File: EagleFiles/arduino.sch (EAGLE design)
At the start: 23 parts, among them IC2 74250N, IC3 74250N, IC4 74250N, J1 AVR_SPI, U1 ATMEGA168

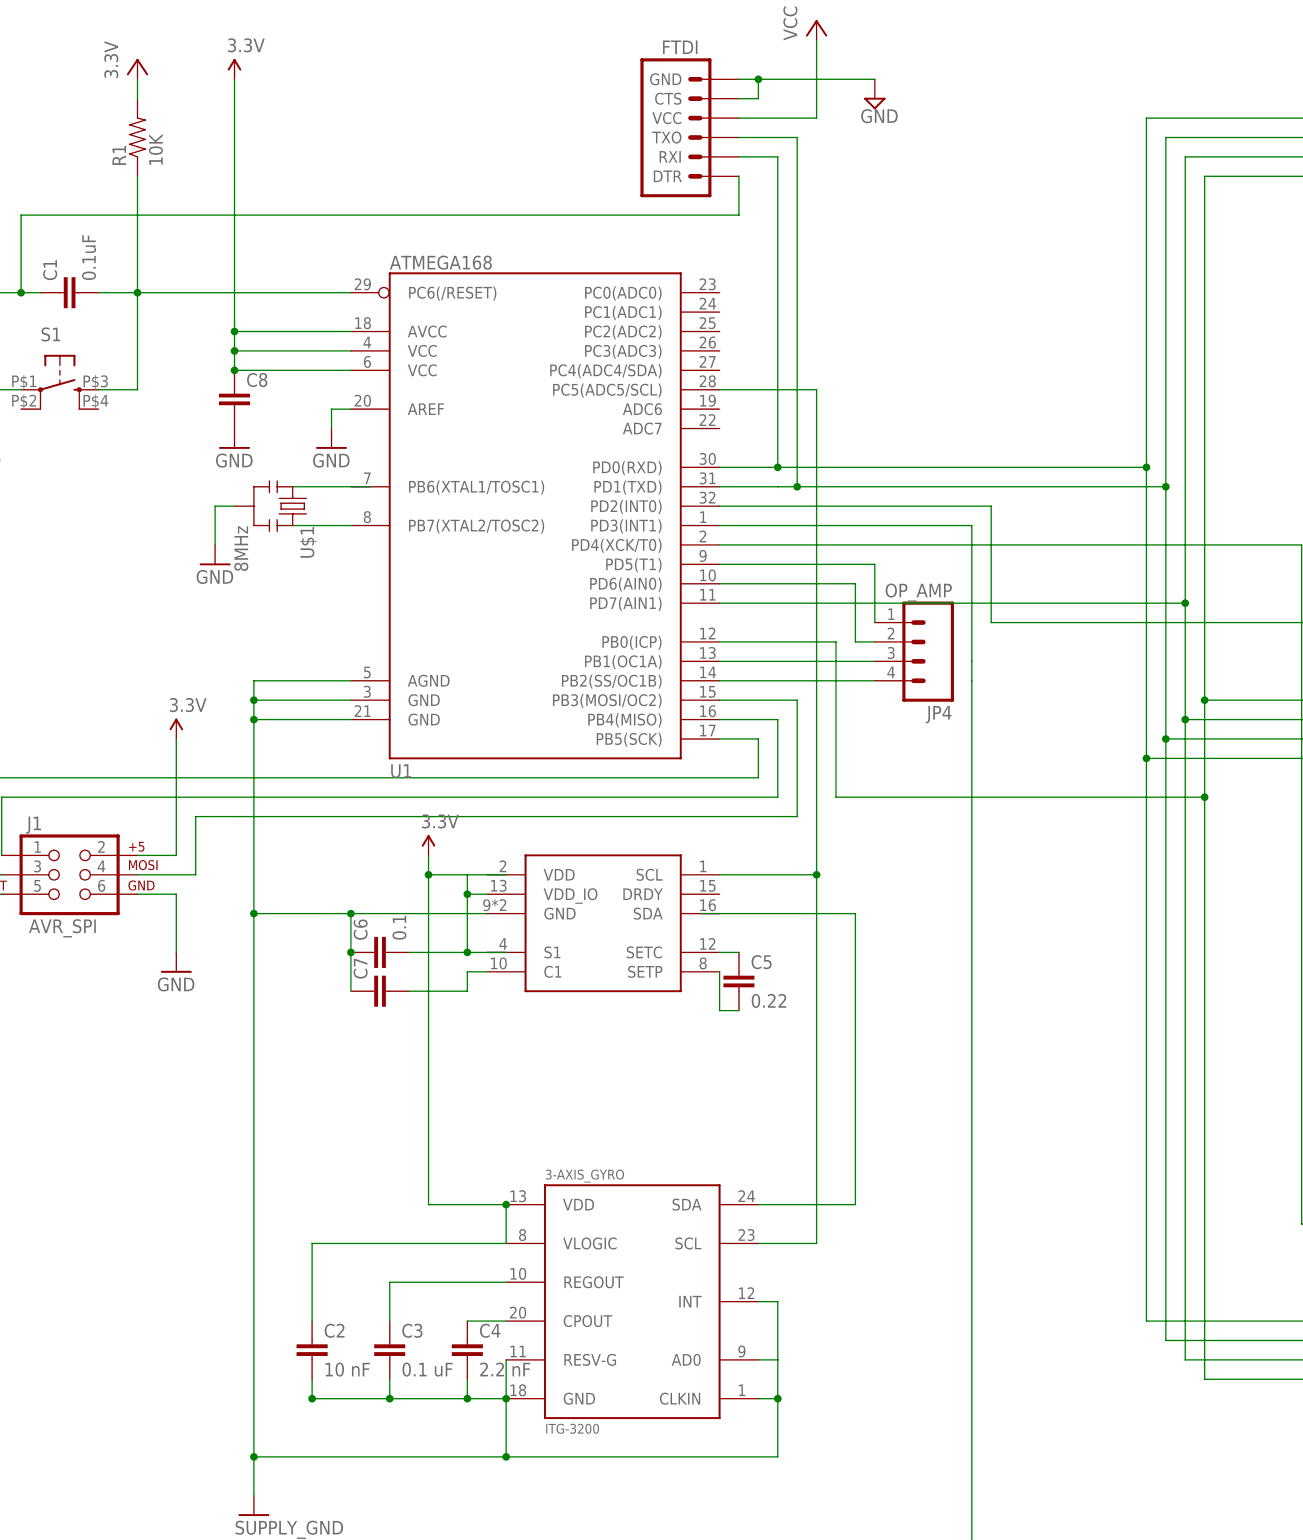
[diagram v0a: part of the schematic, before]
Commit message: made changes suggested by Edrick
- switched ftdi rx/tx times
- added caps to each power line in to ATMEGA
- fixed SDA connection for 12c bus
- fixed gyro connections
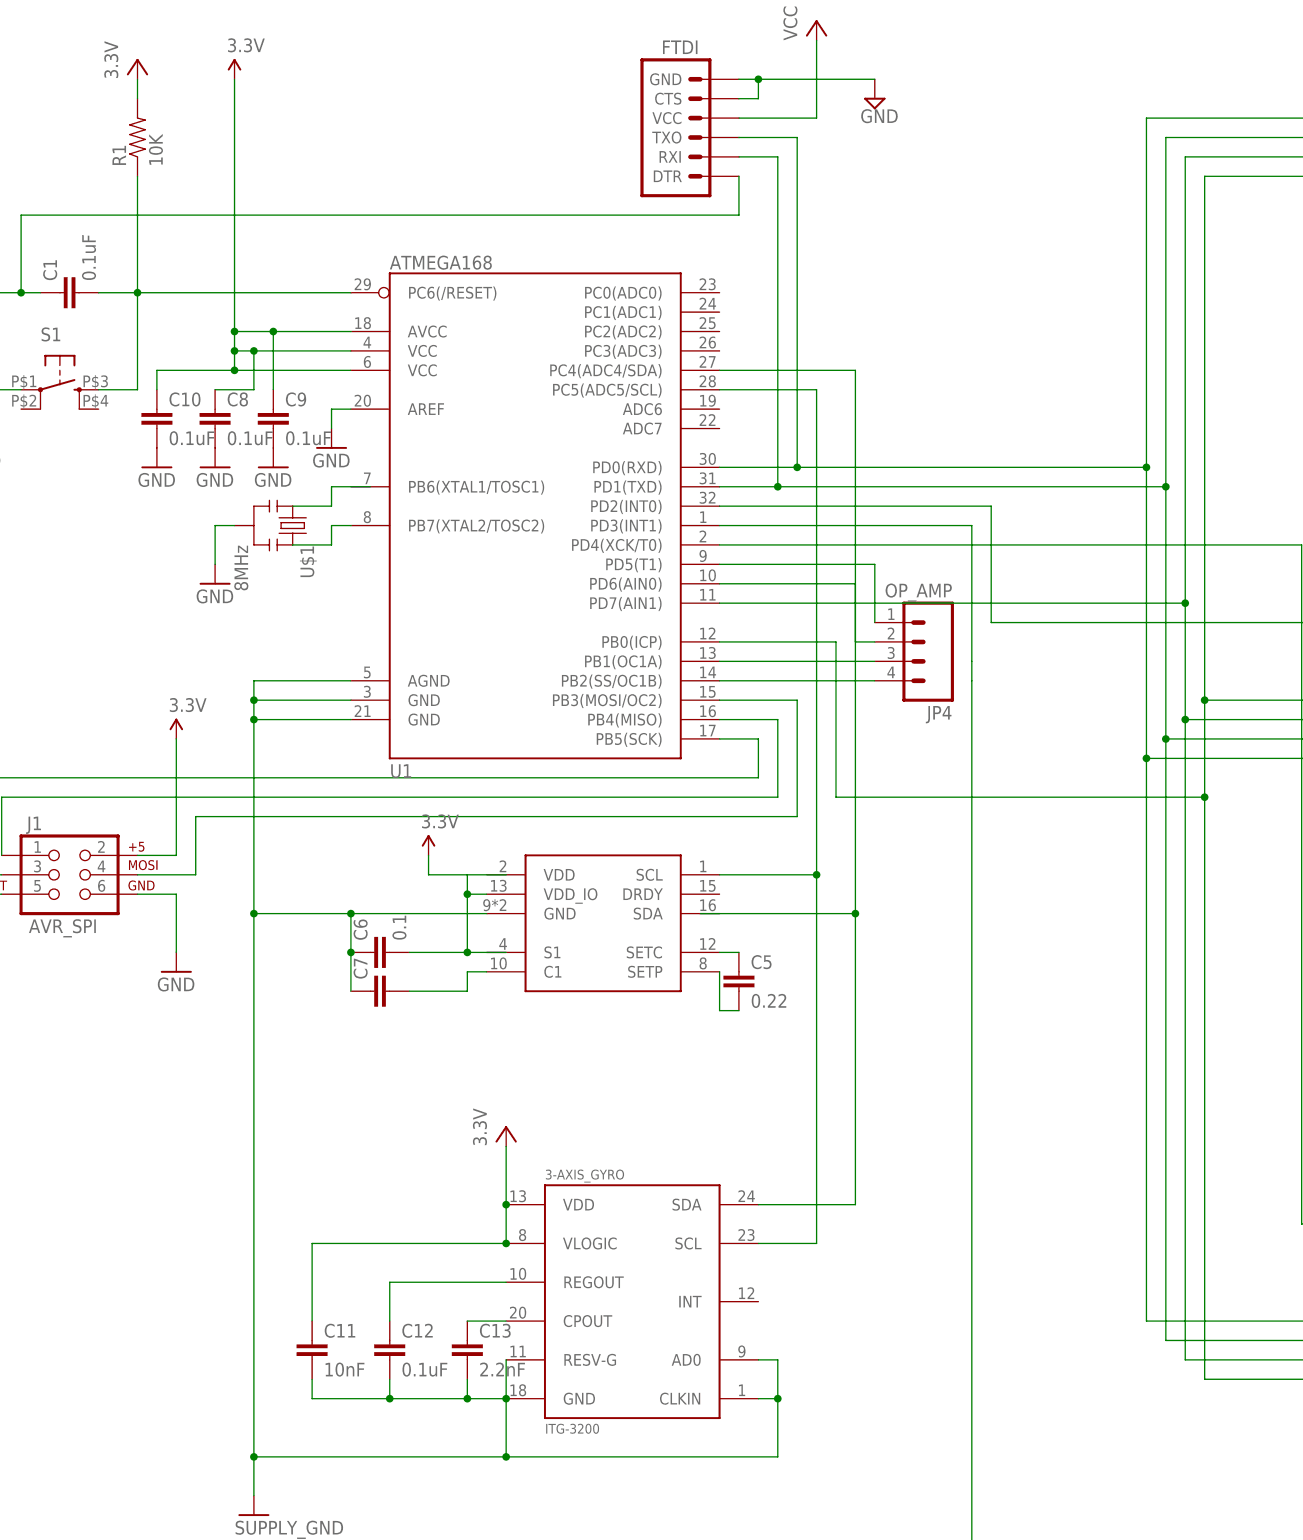
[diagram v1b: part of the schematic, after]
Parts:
- removed C2: 10 nF, SparkFun:CAPPTH
- removed C3: 0.1 uF, SparkFun:CAPPTH
- removed C4: 2.2 nF, SparkFun:CAPPTH
- added C10, C9: 0.1uF, SparkFun:CAP0603-CAP
- added C11: 10nF, SparkFun:CAP0402-CAP
- added C12: 0.1uF, SparkFun:CAP0402-CAP
- added C13: 2.2nF, SparkFun:CAP0402-CAP
- C8: value (none) -> 0.1uF
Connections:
- removed net N$63: FTDI.RXI, IC2A.A, IC3A.A, IC4A.A, U1.PD0(RXD)
- removed net N$66: FTDI.TXO, IC2A.B, IC3A.B, IC4A.B, U1.PD1(TXD)
- new net N$3: FTDI.RXI, IC2A.B, IC3A.B, IC4A.B, U1.PD1(TXD)
- new net N$4: FTDI.TXO, IC2A.A, IC3A.A, IC4A.A, U1.PD0(RXD)
- net GND: now also C10.2, C11.2, C12.2, C13.2, C9.2; no longer 3-AXIS_GYRO.INT, C2.2, C3.2, C4.2
- net N$43: now also U1.PC4(ADC4/SDA)
- net N$64: now also C13.1; no longer C4.1
- net N$65: now also C12.1; no longer C3.1
- net VCC: now also C10.1, C11.1, C9.1; no longer C2.1
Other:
- moved on the sheet: C8, U$1

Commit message: made the fixes
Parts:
- removed IC4: 74250N, 74xx-us:74250N
- added IC1: 4067D, 40xx:4067D
- added R2, R3: 4.7k, SparkFun:RESISTOR
- IC2: value 74250N -> 4067D; device 74xx-us:74250N -> 40xx:4067D
- IC3: value 74250N -> 4067D; device 74xx-eu:74250N -> 40xx:4067D
- JP4: value OP_AMP -> LPF
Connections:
- net GND: now also IC1A.INH, IC2A.INH, IC3A.INH; no longer IC2A.G, IC3A.G, IC4A.G
- net N$1: now also IC1A.X15; no longer IC2A.E15
- net N$10: now also IC1A.X12; no longer IC2A.E12
- net N$11: now also IC1A.X11; no longer IC2A.E11
- net N$12: now also IC1A.X10; no longer IC2A.E10
- net N$13: now also IC1A.X9; no longer IC2A.E9
- net N$14: now also IC1A.X8; no longer IC2A.E8
- net N$15: now also IC1A.X7; no longer IC2A.E7
- net N$16: now also IC1A.X6; no longer IC2A.E6
- net N$17: now also IC1A.X5; no longer IC2A.E5
- net N$18: now also IC1A.X4; no longer IC2A.E4
- net N$19: now also IC1A.X3; no longer IC2A.E3
- net N$2: now also IC1A.C, IC2A.B, IC3A.B; no longer IC2A.C, IC3A.C, IC4A.C
- net N$20: now also IC1A.X2; no longer IC2A.E2
- net N$21: now also IC1A.X1; no longer IC2A.E1
- net N$22: now also IC1A.X0; no longer IC2A.E0
- net N$23: now also IC2A.X15; no longer IC3A.E15
- net N$24: now also IC2A.X14; no longer IC3A.E14
- net N$25: now also IC2A.X13; no longer IC3A.E13
- net N$26: now also IC2A.X12; no longer IC3A.E12
- net N$27: now also IC2A.X11; no longer IC3A.E11
- net N$28: now also IC2A.X10; no longer IC3A.E10
- net N$29: now also IC2A.X9; no longer IC3A.E9
- net N$3: now also IC1A.B, IC2A.C, IC3A.C; no longer IC2A.B, IC3A.B, IC4A.B
- net N$30: now also IC2A.X8; no longer IC3A.E8
- net N$31: now also IC2A.X7; no longer IC3A.E7
- net N$32: now also IC2A.X6; no longer IC3A.E6
- net N$33: now also IC2A.X5; no longer IC3A.E5
- net N$34: now also IC2A.X4; no longer IC3A.E4
- net N$35: now also IC2A.X3; no longer IC3A.E3
- net N$36: now also IC2A.X2; no longer IC3A.E2
- net N$37: now also IC2A.X1; no longer IC3A.E1
- net N$38: now also IC2A.X0; no longer IC3A.E0
- net N$4: now also IC1A.A, IC2A.D, IC3A.D; no longer IC2A.A, IC3A.A, IC4A.A
- net N$41: now also R2.1
- net N$42: now also IC3A.X, U1.PC2(ADC2); no longer IC4A.W, U1.PD3(INT1)
- net N$43: now also R3.1
- net N$46: now also IC3A.X15; no longer IC4A.E15
- net N$47: now also IC3A.X14; no longer IC4A.E14
- net N$48: now also IC3A.X13; no longer IC4A.E13
- net N$49: now also IC3A.X12; no longer IC4A.E12
- net N$5: now also IC1A.X, U1.PC0(ADC0); no longer IC2A.W, U1.PD2(INT0)
- net N$50: now also IC3A.X11; no longer IC4A.E11
- net N$51: now also IC3A.X10; no longer IC4A.E10
- net N$52: now also IC3A.X9; no longer IC4A.E9
- net N$53: now also IC3A.X8; no longer IC4A.E8
- net N$54: now also IC3A.X7; no longer IC4A.E7
- net N$55: now also IC3A.X6; no longer IC4A.E6
- net N$56: now also IC3A.X5; no longer IC4A.E5
- net N$57: now also IC3A.X4; no longer IC4A.E4
- net N$58: now also IC3A.X3; no longer IC4A.E3
- net N$59: now also IC3A.X2; no longer IC4A.E2
- net N$6: now also IC2A.X, U1.PC1(ADC1); no longer IC3A.W, U1.PD4(XCK/T0)
- net N$60: now also IC3A.X1; no longer IC4A.E1
- net N$61: now also IC3A.X0; no longer IC4A.E0
- net N$7: now also IC1A.D, IC2A.A, IC3A.A; no longer IC2A.D, IC3A.D, IC4A.D
- net N$8: now also IC1A.X14; no longer IC2A.E14
- net N$9: now also IC1A.X13; no longer IC2A.E13
- net VCC: now also 3-AXIS_MAG.VDD, R2.2, R3.2
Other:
- moved on the sheet: JP1, JP2, JP3, JP4

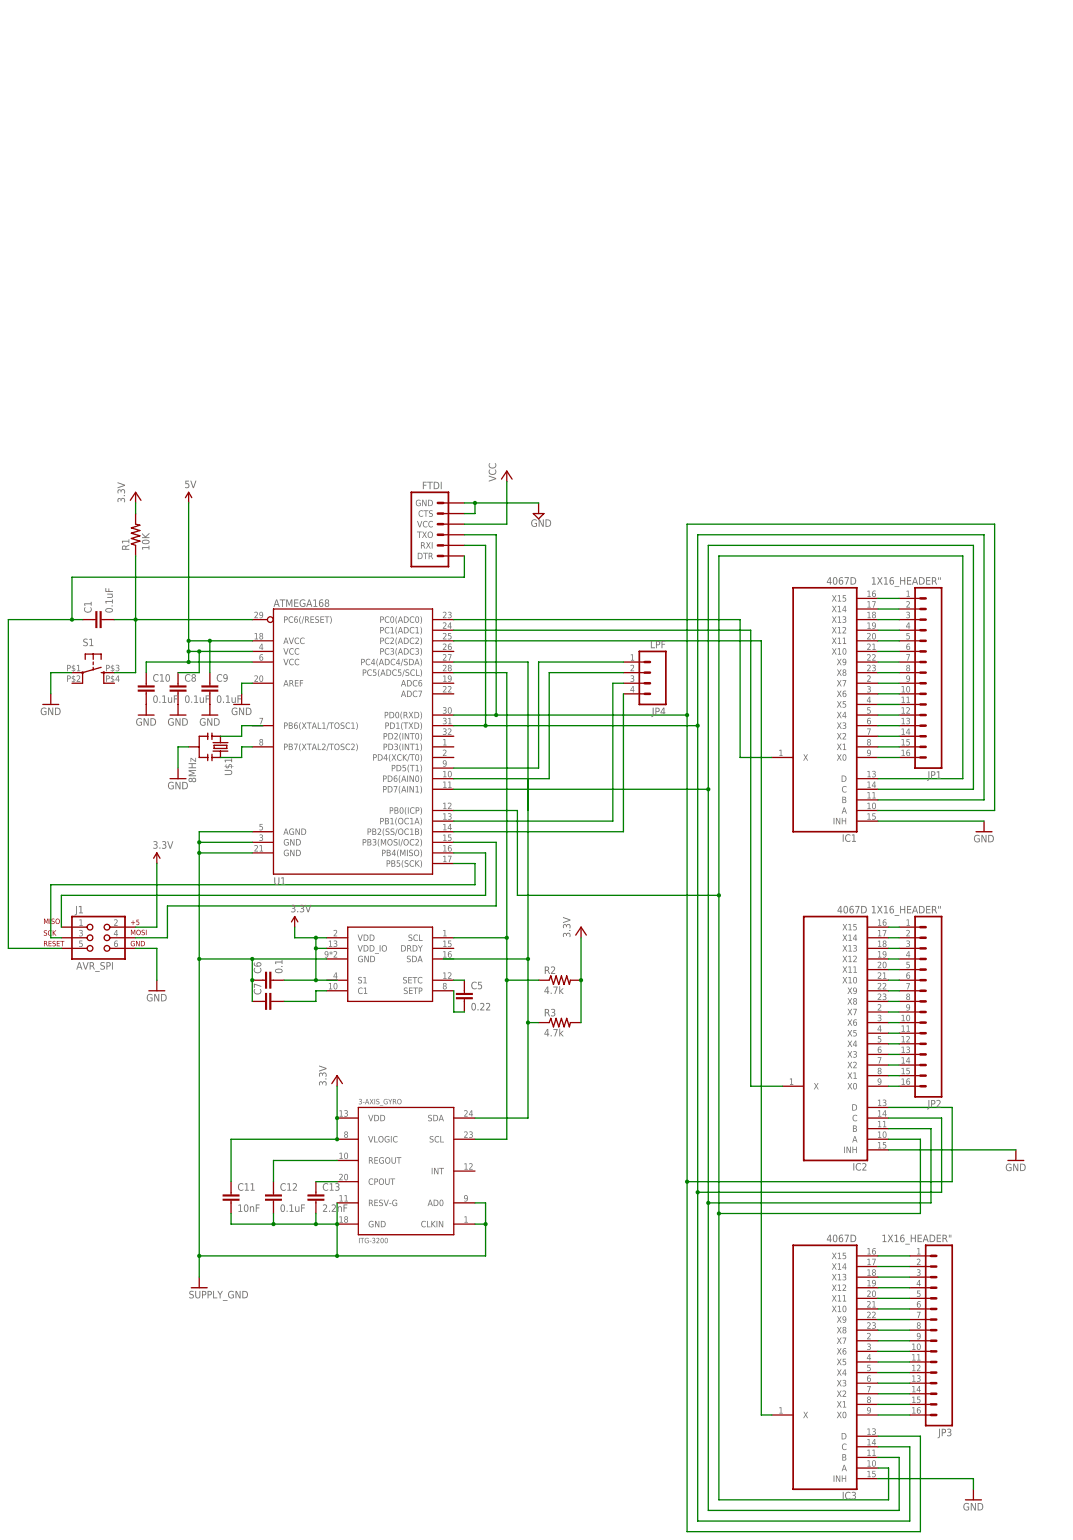
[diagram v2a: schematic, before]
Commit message: added the lpf because forgot that before
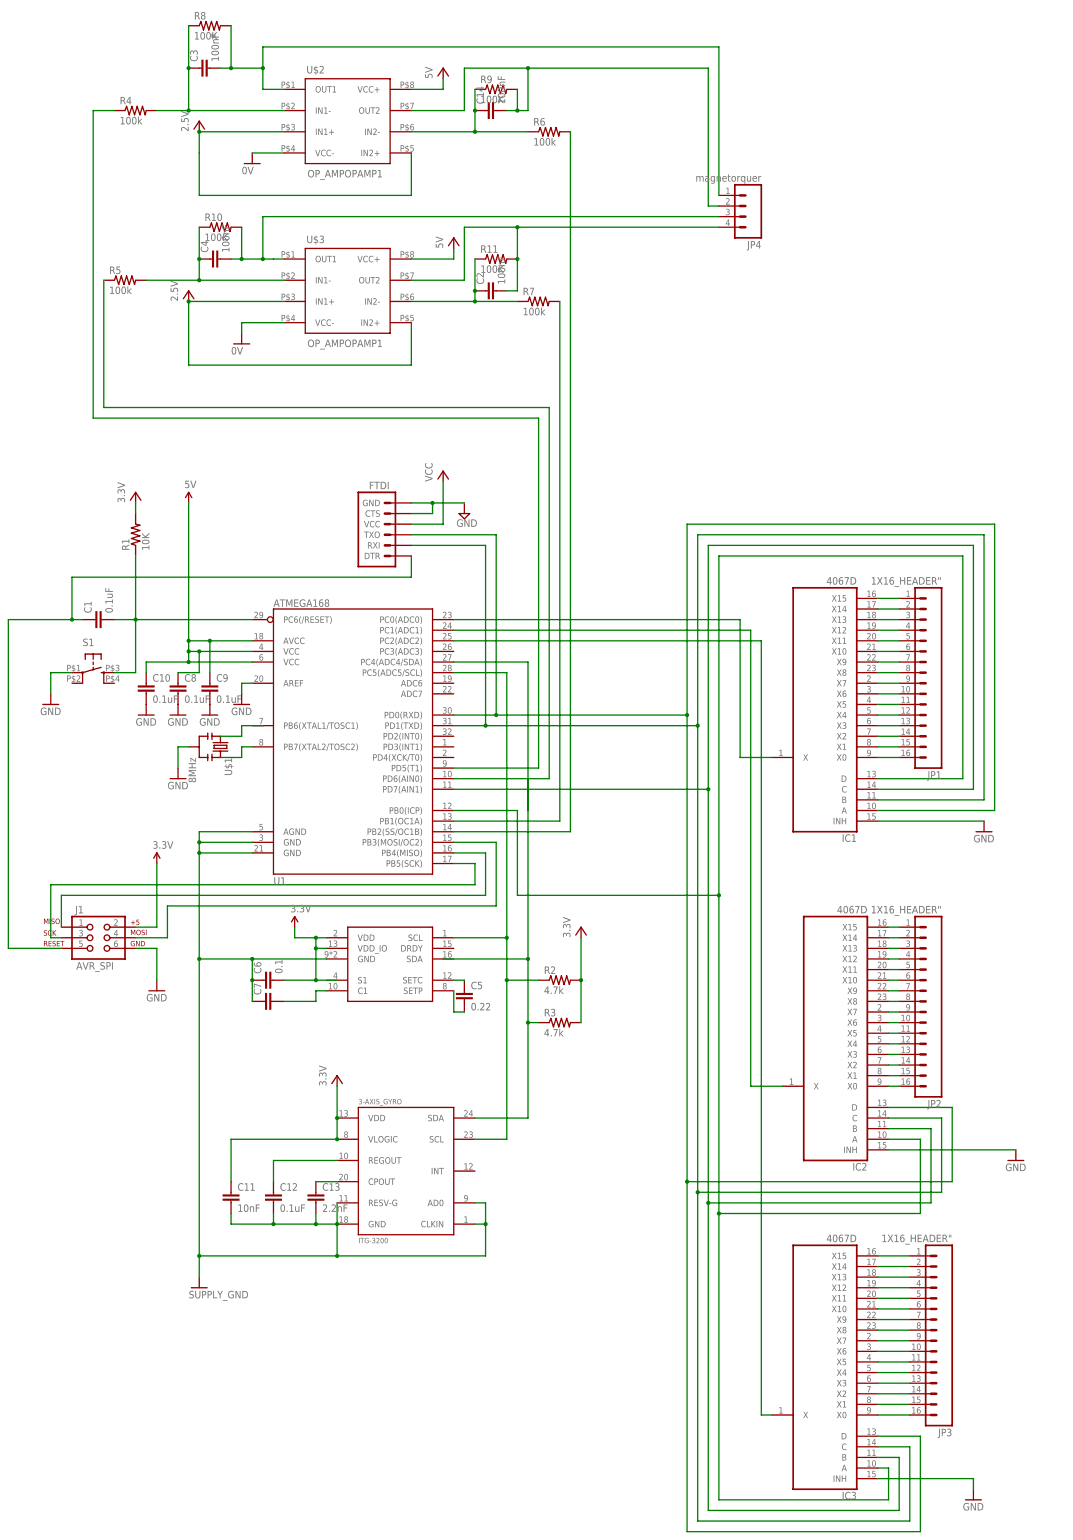
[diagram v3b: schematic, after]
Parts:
- added C14, C2, C3, C4: 100nF, SparkFun:CAP0402-CAP
- added R10, R11, R8, R9: 100K, SparkFun:RESISTOR
- added R4, R5, R6, R7: 100k, SparkFun:RESISTOR
- added U$2, U$3: OP_AMPOPAMP1, watsat:OP_AMPOPAMP1
- JP4: value LPF -> magnetorquer
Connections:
- new net N$66: C3.2, JP4.1, R8.2, U$2.OUT1
- new net N$76: C4.1, R10.1, R5.2, U$3.IN1-
- new net N$77: C14.1, R6.1, R9.1, U$2.IN2-
- new net N$78: C2.1, R11.1, R7.1, U$3.IN2-
- new net N$79: C4.2, JP4.3, R10.2, U$3.OUT1
- new net N$83: C2.2, JP4.4, R11.2, U$3.OUT2
- new net N$84: C3.1, R4.2, R8.1, U$2.IN1-
- new net N$85: C14.2, JP4.2, R9.2, U$2.OUT2
- net GND: now also U$2.VCC-, U$3.VCC-
- net N$63: now also R5.1; no longer JP4.2
- net N$72: now also R7.2; no longer JP4.3
- net N$73: now also R4.1; no longer JP4.1
- net N$75: now also R6.2; no longer JP4.4
- net VCC: now also U$2.IN1+, U$2.IN2+, U$2.VCC+, U$3.IN1+, U$3.IN2+, U$3.VCC+
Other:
- moved on the sheet: FTDI, JP4

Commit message: made some changes?
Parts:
- C6: value 0.1 -> 0.1uF
- C7: value (none) -> 0.1uF
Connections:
- new net N$80: FTDI.TXO, U1.PD0(RXD)
- new net N$81: FTDI.RXI, U1.PD1(TXD)
- net N$3: now also U1.PD2(INT0); no longer FTDI.RXI, U1.PD1(TXD)
- net N$4: now also U1.PD3(INT1); no longer FTDI.TXO, U1.PD0(RXD)
- net N$43: now also 3-AXIS_MAG.SDA
- net N$69: now also U1.PB6(XTAL1/TOSC1)
- net VCC: now also 3-AXIS_MAG.S1
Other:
- moved on the sheet: IC1
